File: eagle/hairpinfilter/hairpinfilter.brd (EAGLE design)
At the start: 45.6 x 43.2 mm, 7 parts

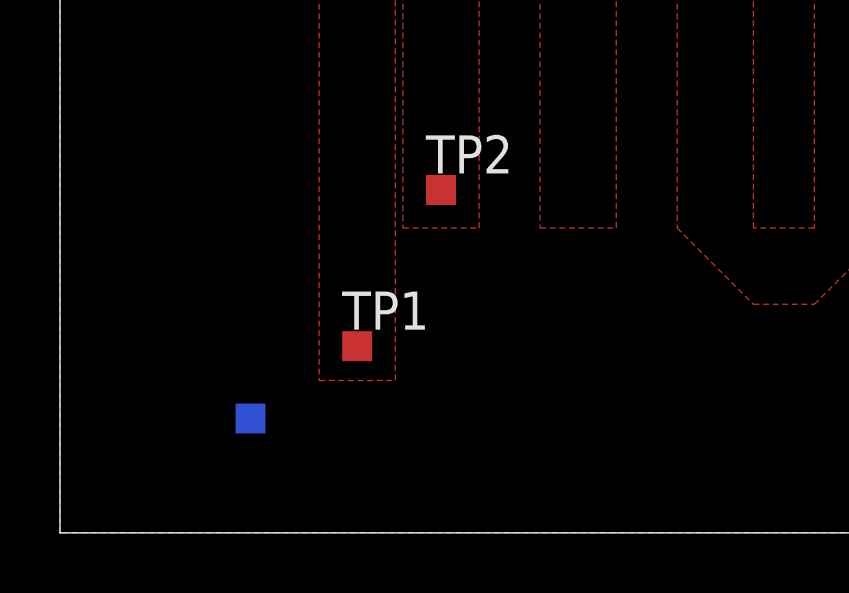
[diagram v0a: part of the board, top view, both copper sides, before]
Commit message: cleanup examples and doc
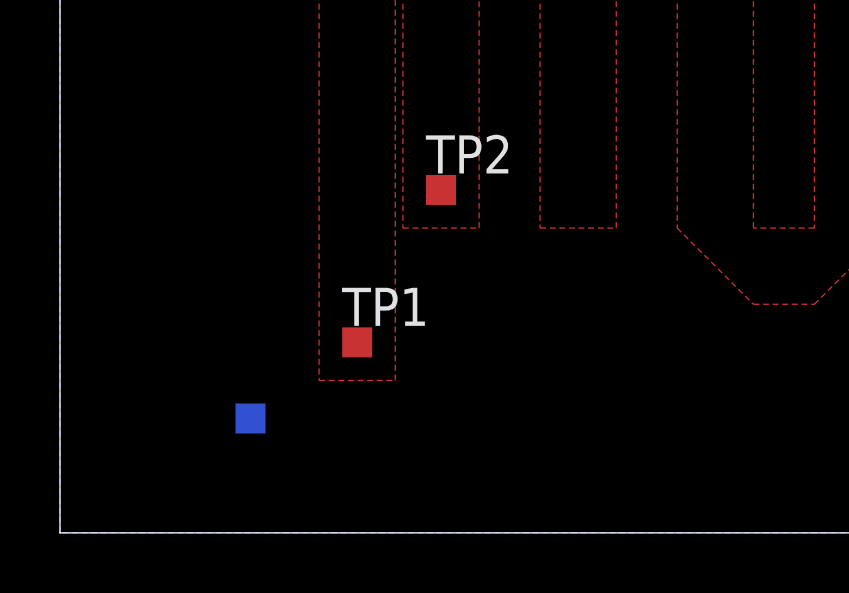
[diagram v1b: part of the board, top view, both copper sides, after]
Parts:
- moved TP1 0.13 mm to (9.91, 6.35)
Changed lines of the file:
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@@
 </autorouter>
 <elements>
-<element name="TP1" library="testpad" package="TP10SQ" value="TPTP10SQ" x="9.906" y="6.223">
-<attribute name="TP_SIGNAL_NAME" value="" x="9.906" y="6.223" size="1.778" layer="27" display="off"/>
+<element name="TP1" library="testpad" package="TP10SQ" value="TPTP10SQ" x="9.906" y="6.35">
+<attribute name="TP_SIGNAL_NAME" value="" x="9.906" y="6.35" size="1.778" layer="27" display="off"/>
 </element>
 <element name="TP2" library="testpad" package="TP10SQ" value="TPTP10SQ" x="12.7" y="11.43">
